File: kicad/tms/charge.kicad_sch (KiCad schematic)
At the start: 48 parts, among them K1 AZ9861-1C-24DC2R1, Q2 NPN, T1 Transformer_1P_1S, U1 VO2611, U10 VO2611, U3 LM393, U7 IL300, U8 UA741, U9 UA741

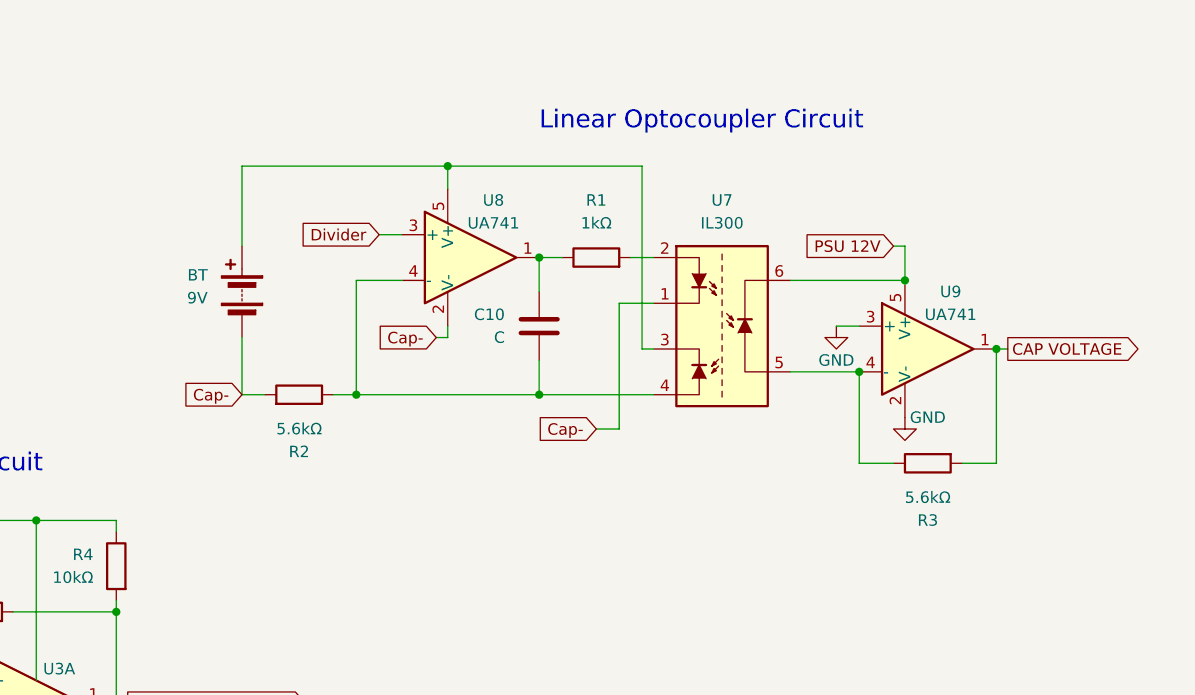
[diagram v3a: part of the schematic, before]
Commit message: Fixed the linear optocoupler schematic
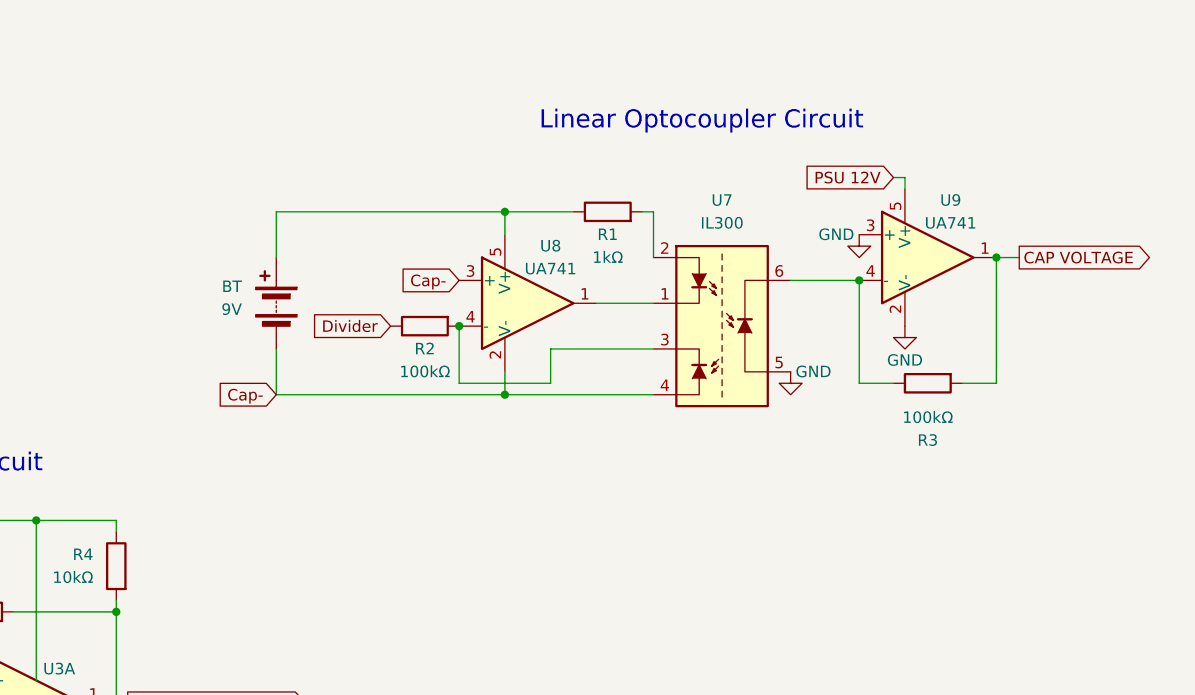
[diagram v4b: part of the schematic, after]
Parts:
- removed C10: C, symbol Device:C
- R2, R3: value 5.6kΩ -> 100kΩ
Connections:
- net Cap-: now also U7.4, U8.3 (+); no longer R2.2, U7.1
- net Divider: now also R2.1; no longer U8.3 (+)
- net GND: now also U7.5
- net PSU 12V: no longer U7.6
- net at BT.1 (+), U8.5 (V+): now also R1.1; no longer U7.3
- net at R3.1, U9.4 (-): now also U7.6; no longer U7.5
- net at U8.1: now also U7.1; no longer R1.1
- new net: R2.2, U7.3, U8.4 (-)
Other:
- moved on the sheet: BT, R1, R2, R3, U8, U9

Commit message: Fixed TMS schematic
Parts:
- added C14: 0.1uF, symbol Device:C
- added C15: 22 pF, symbol Device:C
- added R23, R24: 1.2kΩ, symbol Device:R
- added U9: VO2611, Package_DIP:DIP-8_W7.62mm, symbol Isolator:VO2611
- R14: renamed from R20; value 1kΩ -> 1.2kΩ
- renumbered BT to BT1, C13 to C10, C14 to C11, C11 to C12, C12 to C13, R11 to R13, R12 to R15, R13 to R16, R14 to R17, R15 to R18, R5 to R19, R17 to R20, R4 to R21, R16 to R22, R2 to R25, R1 to R26, R3 to R27, U1 to U3, U10 to U4, U8 to U5, U7 to U6, U9 to U7, U3 to U8
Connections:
- net +5V: now also C14.1, R24.1, U9.7 (EN), U9.8 (VCC)
- net COMPARATOR STOP: now also C15.1, R24.2, U9.6 (VO); no longer R19.1, R20.2, R21.2, U8.1
- net GND: now also C14.2, C15.2, U9.5 (GND)
- net at BT1.1 (+), R21.1, RV1.1: now also R23.1
- new net: R23.2, U9.2 (A)
- new net COMPARATOR STOP HV: R19.1, R20.2, R21.2, U8.1, U9.3 (C)
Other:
- moved on the sheet: BT1, R20, R21, R22, RV1, U8A

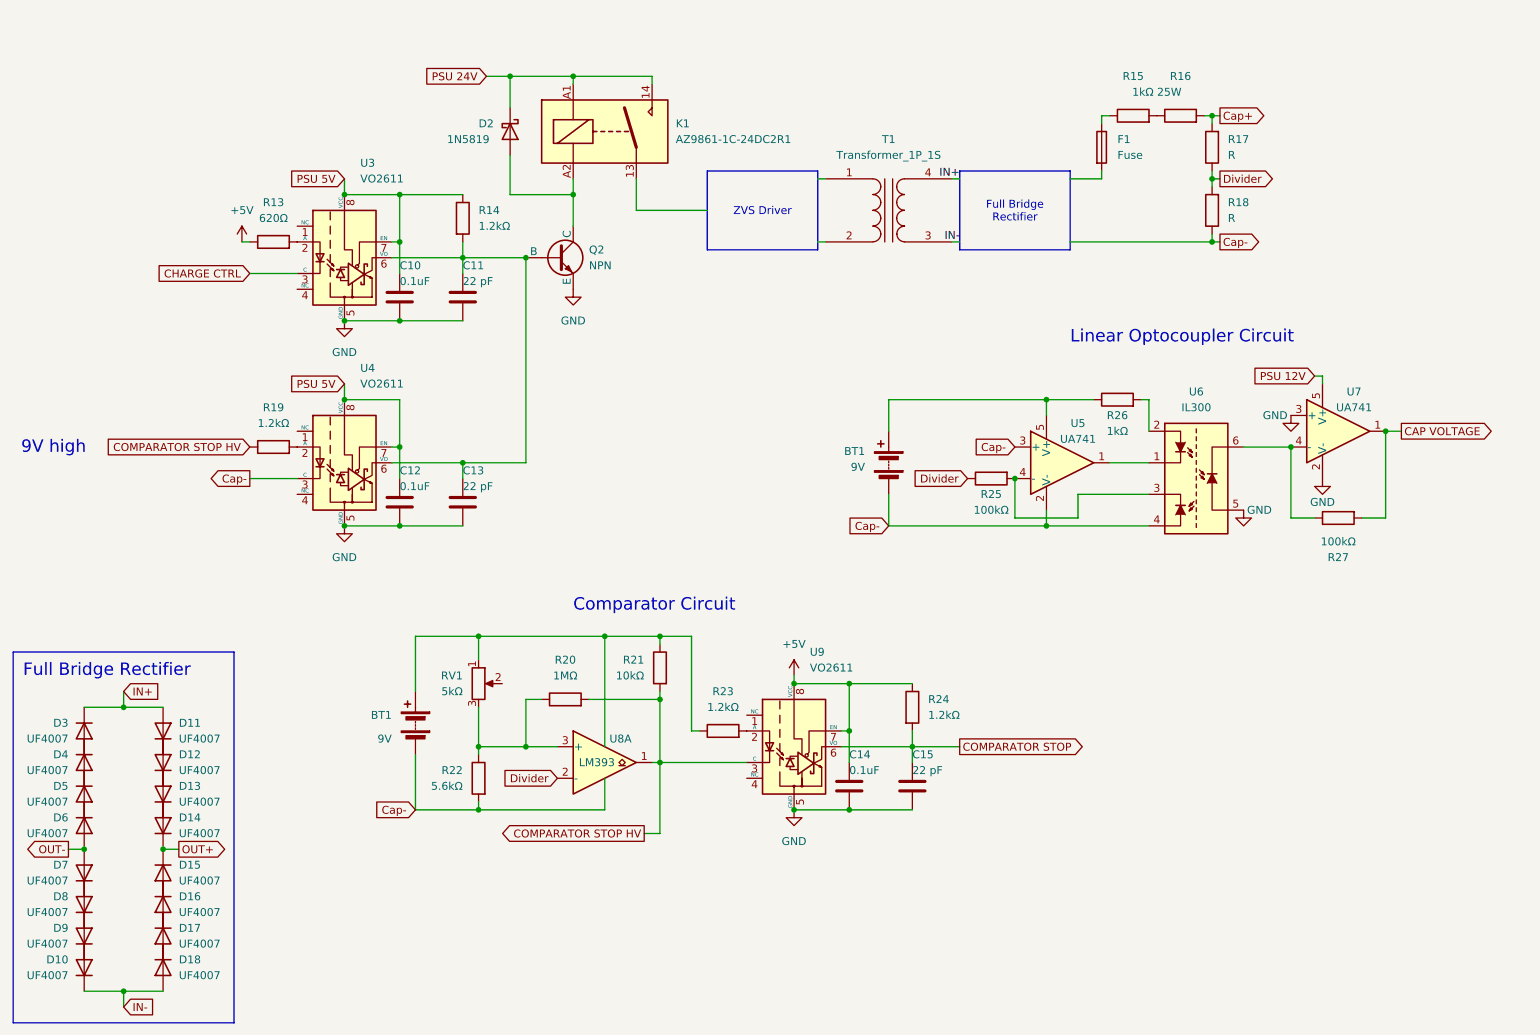
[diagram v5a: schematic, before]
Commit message: Schematic changes
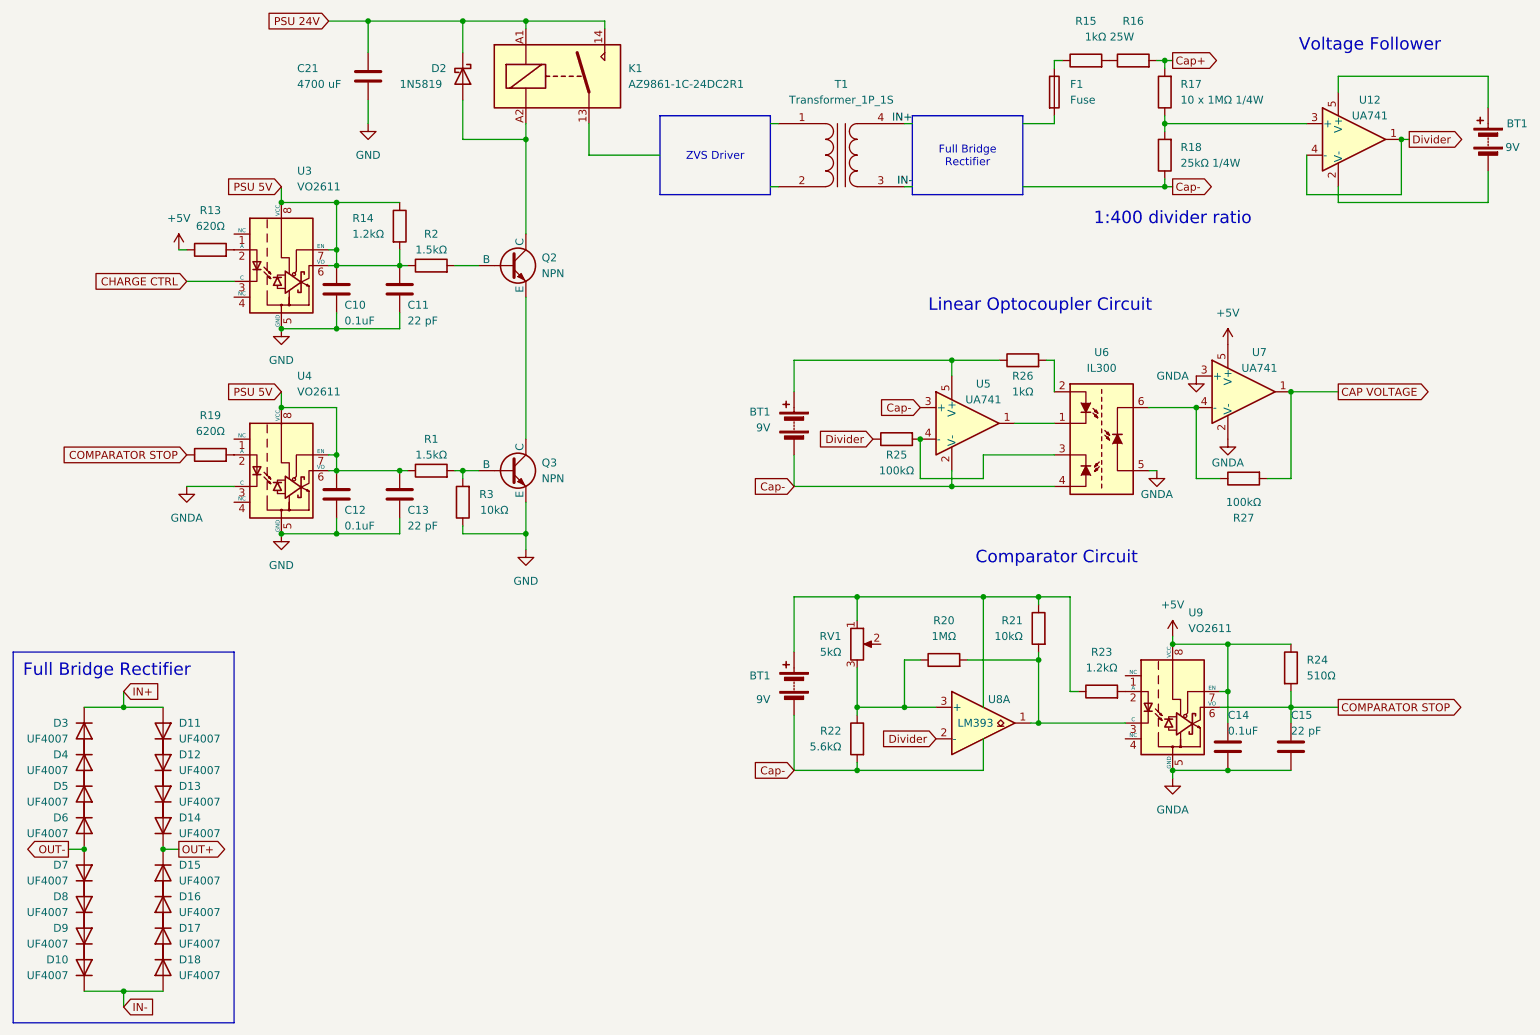
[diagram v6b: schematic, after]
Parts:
- added BT1: 9V, symbol Device:Battery
- added C21: 4700 uF, symbol Device:C
- added Q3: NPN, symbol Simulation_SPICE:NPN
- added R1, R2: 1.5kΩ, symbol Device:R
- added R3: 10kΩ, symbol Device:R
- added U12: UA741, Package_TO_SOT_SMD:SOT-23-5, symbol Amplifier_Operational:ADA4610-1xRJ
- R17: value R -> 10 x 1MΩ 1/4W
- R18: value R -> 25kΩ 1/4W
- R19: value 1.2kΩ -> 620Ω
- R24: value 1.2kΩ -> 510Ω
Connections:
- net PSU 12V is gone; now on net +5V: U7.5 (V+)
- net COMPARATOR STOP: now also R19.1
- net Cap-: no longer U4.3 (C)
- net Divider: now also U12.1, U12.4 (-); no longer R17.1, R18.2
- net GND: now also C21.2, Q3.3 (E), R3.1; no longer C14.2, C15.2, Q2.3 (E), U6.5, U7.2 (V-), U7.3 (+), U9.5 (GND)
- net PSU 24V: now also C21.1
- net PSU 5V: now also C11.1, C13.1, R14.2, U3.6 (VO), U4.6 (VO), R1.1, R2.1
- net COMPARATOR STOP HV: no longer names the net of R20.2, R21.2, U8.1, U9.3 (C)
- net COMPARATOR STOP HV: no longer R19.1
- new net: Q3.2 (B), R1.2, R3.2
- new net: Q2.2 (B), R2.2
- new net: BT1.2 (-), U12.2 (V-)
- new net: R17.1, R18.2, U12.3 (+)
- new net: BT1.1 (+), U12.5 (V+)
- new net: Q2.3 (E), Q3.1 (C)
- new net GNDA: C14.2, C15.2, U4.3 (C), U6.5, U7.2 (V-), U7.3 (+), U9.5 (GND)
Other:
- note added: "1:400 divider ratio"
- note added: "Voltage Follower"
- note removed: "9V high"
- moved on the sheet: BT1, C10, C11, C12, C13, C14, C15, D2, F1, K1, Q2, R13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
